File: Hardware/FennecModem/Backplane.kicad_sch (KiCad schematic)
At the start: 4 parts, among them U301 NCP1117-12_SOT223

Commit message: Route!
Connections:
- net SPI_SDO: now reaches U302.17 (SPI_SD0)
- no-connect marks 12 -> 11
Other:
- moved on the sheet: C302, C303, U301, U302

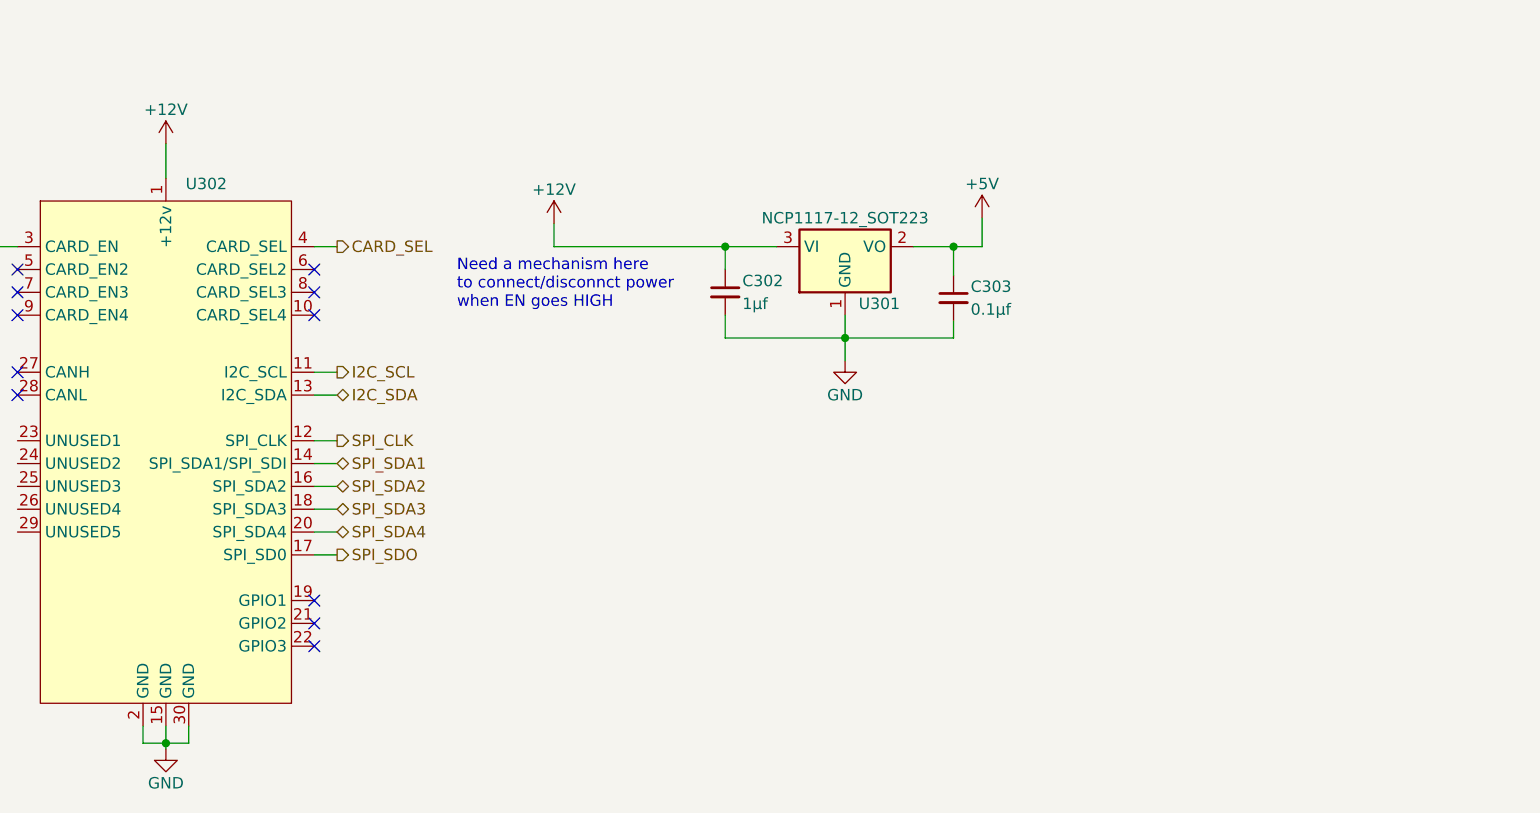
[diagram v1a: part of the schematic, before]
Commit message: Change all power switching
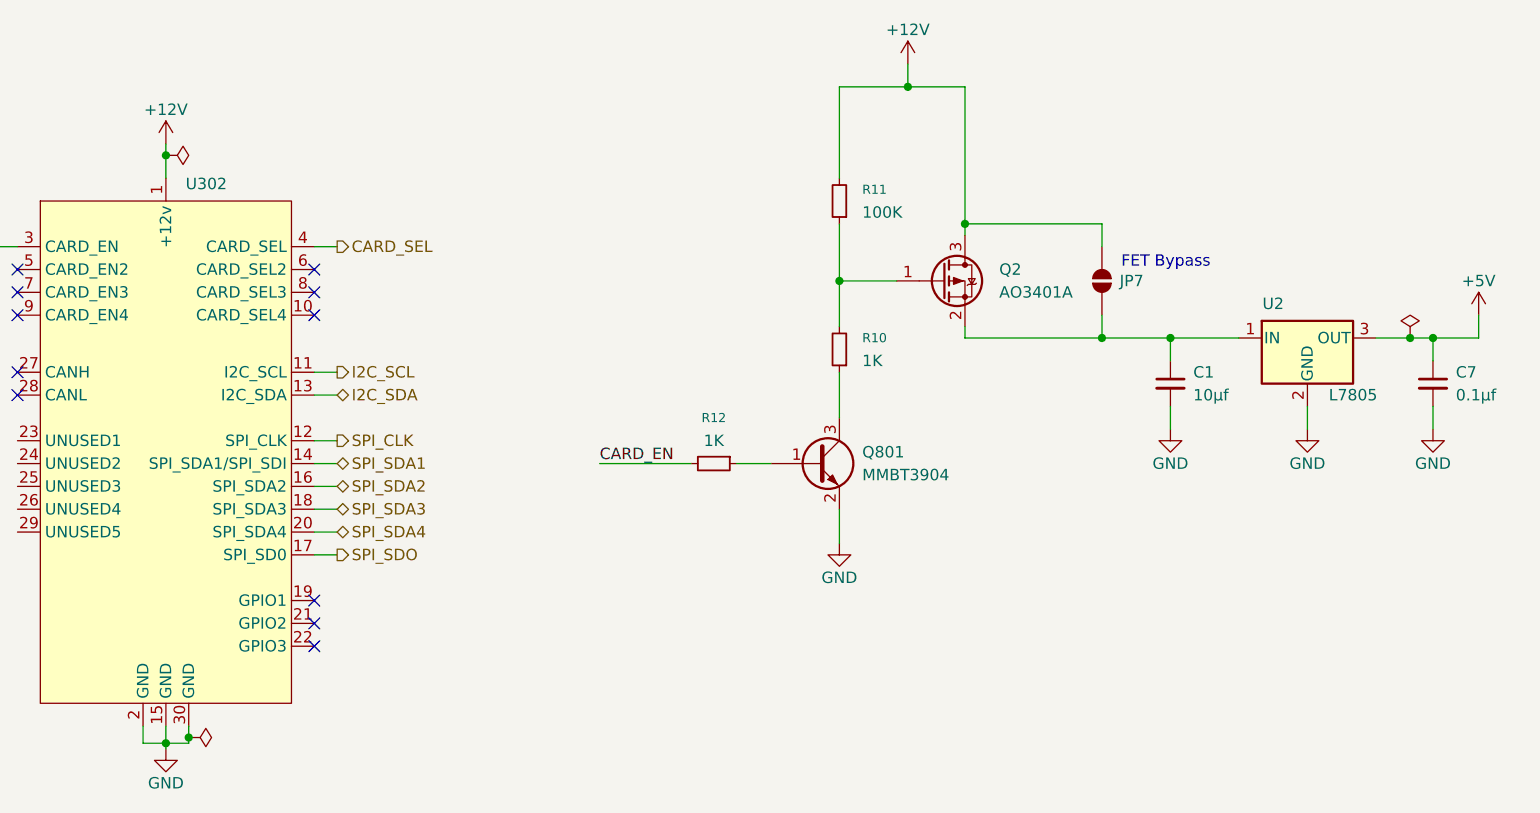
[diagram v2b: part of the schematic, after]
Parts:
- removed C302: 1μf, Capacitor_SMD:C_0805_2012Metric, symbol Device:C_Small
- removed C303: 0.1μf, Capacitor_SMD:C_0805_2012Metric, symbol Device:C_Small
- removed U301: NCP1117-12_SOT223, Package_TO_SOT_SMD:SOT-223-3_TabPin2, symbol Regulator_Linear:NCP1117-12_SOT223
- added C1: 10μf, Capacitor_SMD:C_0805_2012Metric, symbol Device:C_Small
- added C7: 0.1μf, Capacitor_SMD:C_0805_2012Metric, symbol Device:C_Small
- added JP7: SolderJumper_2_Open, Jumper:SolderJumper-2_P1.3mm_Open_TrianglePad1.0x1.5mm, symbol Jumper:SolderJumper_2_Open
- added Q2: AO3401A, Package_TO_SOT_SMD:SOT-23, symbol Transistor_FET:AO3401A
- added Q801: MMBT3904, Package_TO_SOT_SMD:SOT-23, symbol Transistor_BJT:MMBT3904
- added R10, R12: 1K, Resistor_SMD:R_0805_2012Metric, symbol Device:R_Small
- added R11: 100K, Resistor_SMD:R_0805_2012Metric, symbol Device:R_Small
- added U2: L7805, Package_TO_SOT_THT:TO-220-3_Horizontal_TabDown, symbol Regulator_Linear:L7805
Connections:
- net +12V: now also JP7.1 (A), Q2.3 (D), R11.2
- net +5V: now also C7.1, U2.3 (OUT)
- net CARD_EN: now also R12.2
- net GND: now also C1.2, C7.2, Q801.2 (E), U2.2 (GND)
- new net: Q801.3 (C), R10.1
- new net: Q2.1 (G), R10.2, R11.1
- new net: Q801.1 (B), R12.1
- new net: C1.1, JP7.2 (B), Q2.2 (S), U2.1 (IN)
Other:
- note added: "FET Bypass"
- note removed: "Need a mechanism here to connect/disconnct power when EN goes HIGH"

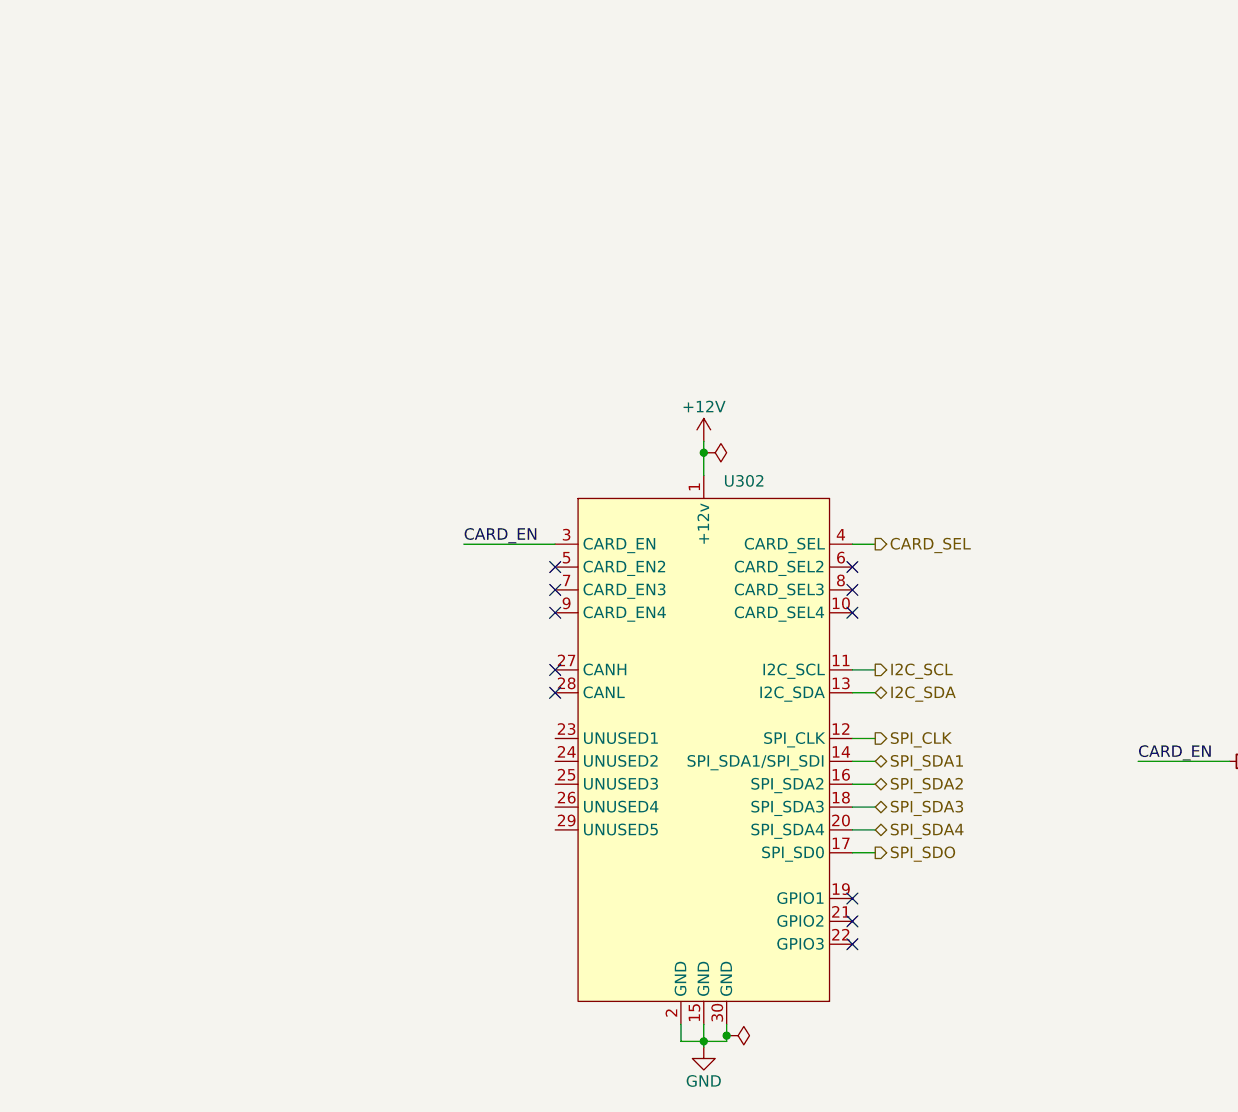
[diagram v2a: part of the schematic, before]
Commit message: add jumpers and bump kicad libs
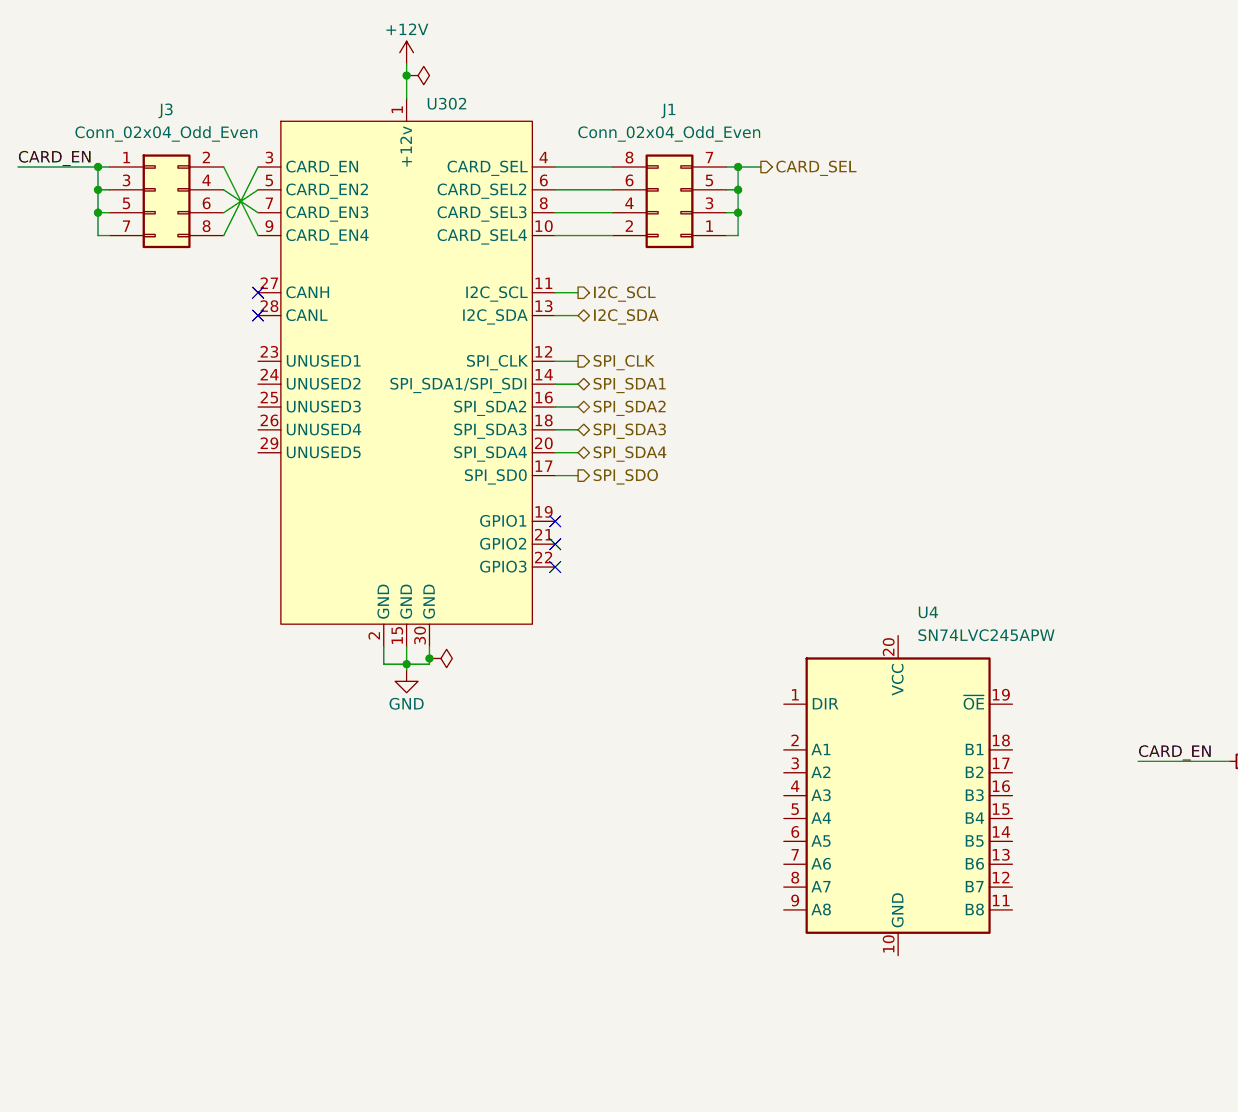
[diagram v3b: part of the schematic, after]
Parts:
- added J1, J3: Conn_02x04_Odd_Even, Connector_PinHeader_2.54mm:PinHeader_2x04_P2.54mm_Vertical, symbol Connector_Generic:Conn_02x04_Odd_Even
- added U4: SN74LVC245APW, Package_SO:TSSOP-20_4.4x6.5mm_P0.65mm, symbol Logic_LevelTranslator:SN74LVC245APW
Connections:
- net CARD_EN: now also J3.1 (Pin_1), J3.3 (Pin_3), J3.5 (Pin_5), J3.7 (Pin_7); no longer U302.3 (CARD_EN)
- net CARD_SEL: now also J1.1 (Pin_1), J1.3 (Pin_3), J1.5 (Pin_5), J1.7 (Pin_7); no longer U302.4 (CARD_SEL)
- net at U302.10 (CARD_SEL4): now also J1.2 (Pin_2)
- net at U302.5 (CARD_EN2): now also J3.6 (Pin_6)
- net at U302.6 (CARD_SEL2): now also J1.6 (Pin_6)
- net at U302.7 (CARD_EN3): now also J3.4 (Pin_4)
- net at U302.8 (CARD_SEL3): now also J1.4 (Pin_4)
- net at U302.9 (CARD_EN4): now also J3.2 (Pin_2)
- new net: J3.8 (Pin_8), U302.3 (CARD_EN)
- new net: J1.8 (Pin_8), U302.4 (CARD_SEL)
- no-connect marks 11 -> 5
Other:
- moved on the sheet: U302

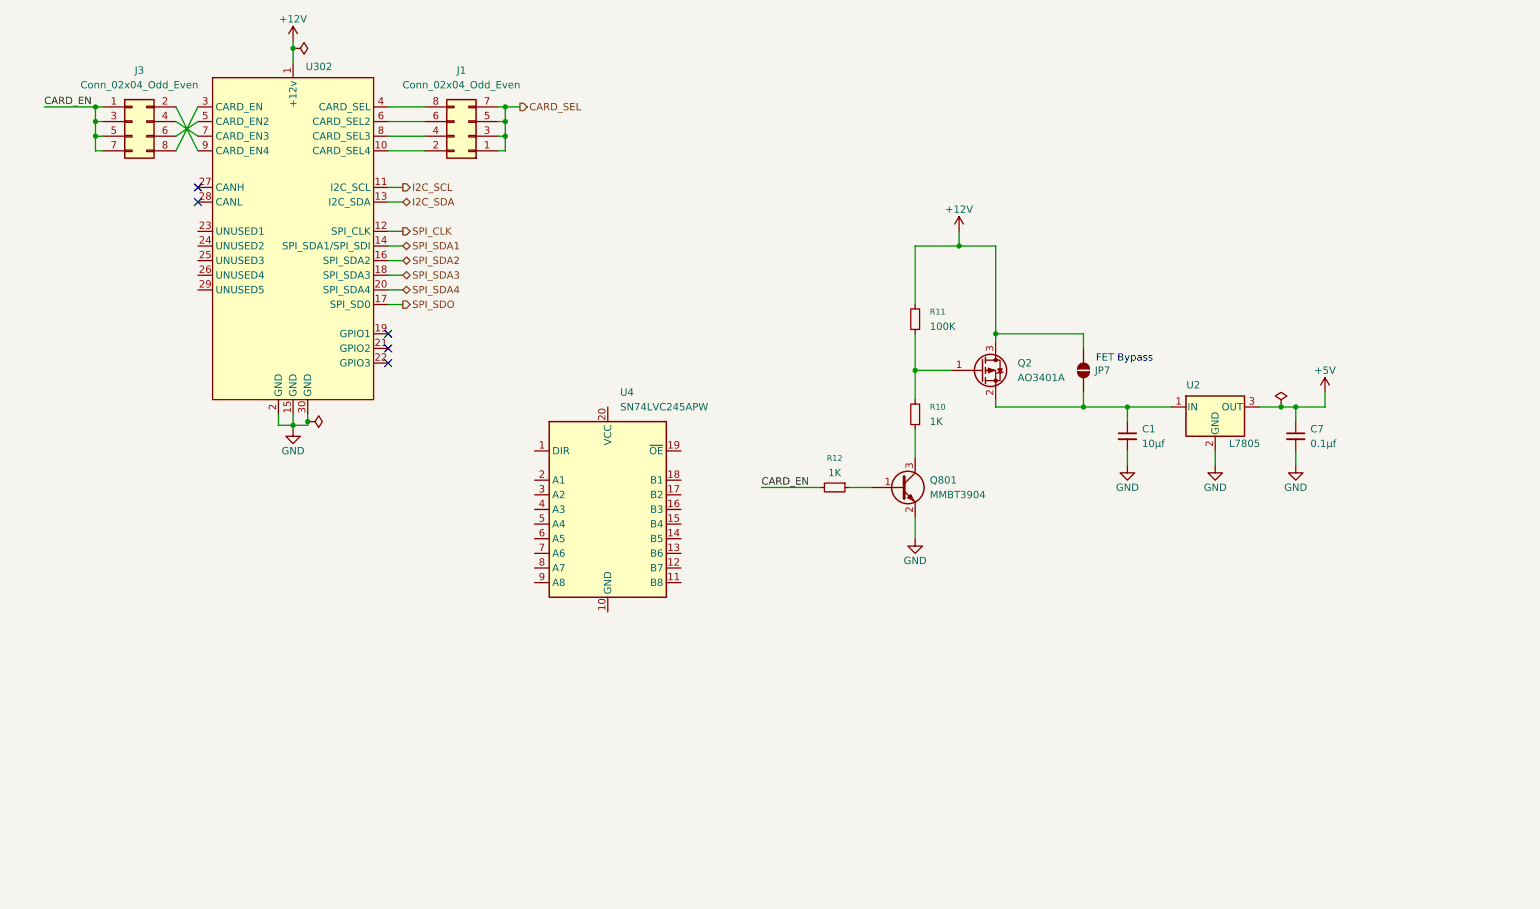
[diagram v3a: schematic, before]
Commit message: Add all nets
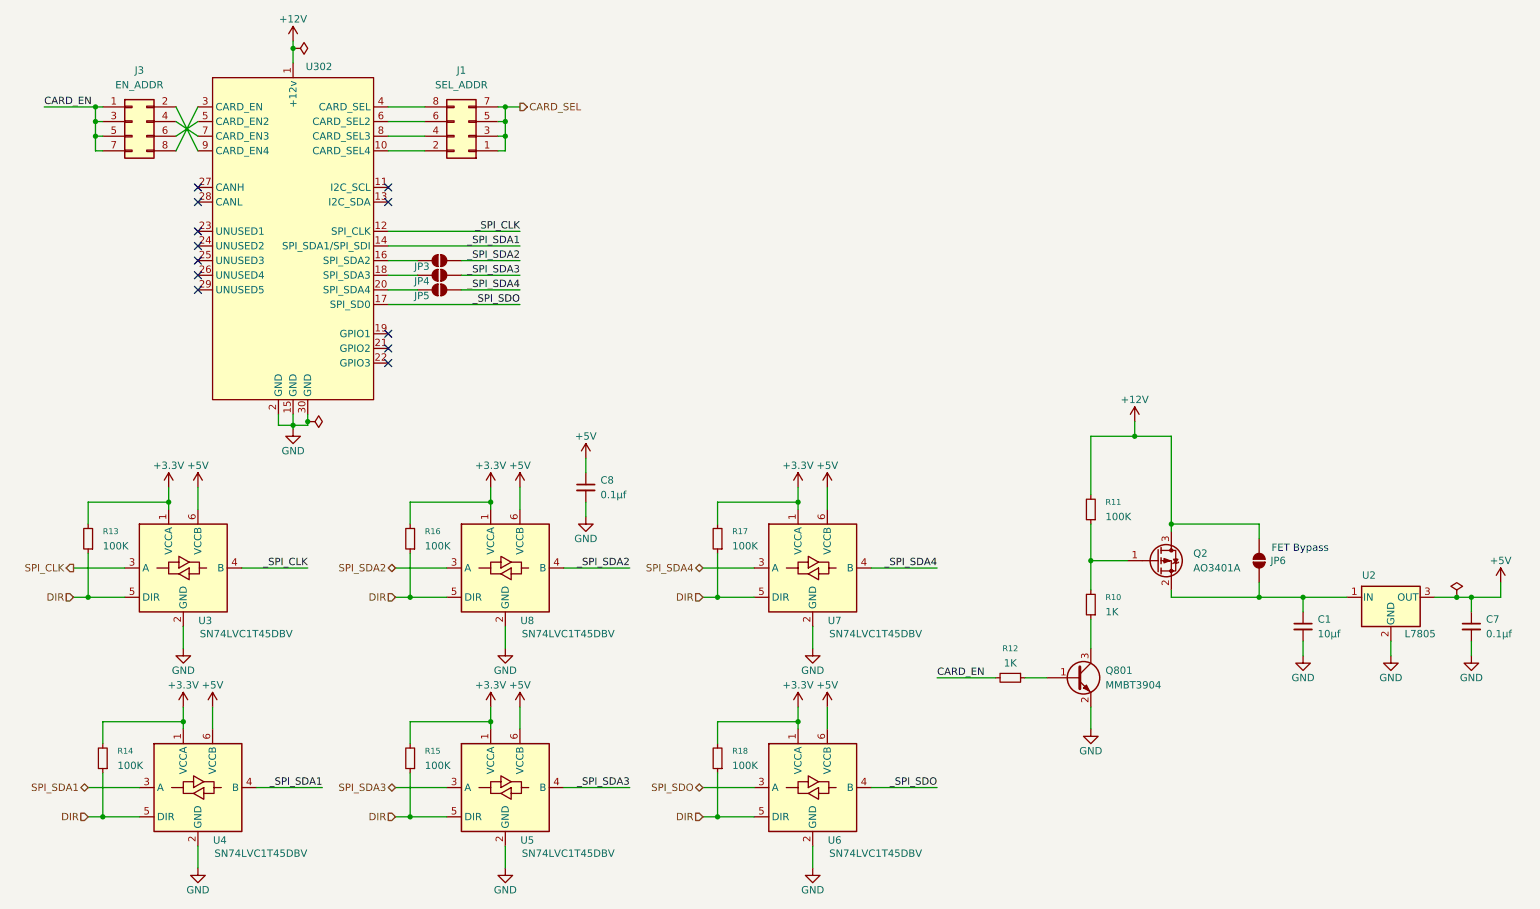
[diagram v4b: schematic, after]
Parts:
- removed U4: SN74LVC245APW, Package_SO:TSSOP-20_4.4x6.5mm_P0.65mm, symbol Logic_LevelTranslator:SN74LVC245APW
- added C8: 0.1μf, Capacitor_SMD:C_0805_2012Metric, symbol Device:C_Small
- added JP3, JP4, JP5: SolderJumper_2_Open, Jumper:SolderJumper-2_P1.3mm_Open_TrianglePad1.0x1.5mm, symbol Jumper:SolderJumper_2_Open
- added R13, R14, R15, R16, R17, R18: 100K, Resistor_SMD:R_0805_2012Metric, symbol Device:R_Small
- added U3, U4, U5, U6, U7, U8: SN74LVC1T45DBV, Package_TO_SOT_SMD:SOT-23-6, symbol Logic_LevelTranslator:SN74LVC1T45DBV
- J1: value Conn_02x04_Odd_Even -> SEL_ADDR
- J3: value Conn_02x04_Odd_Even -> EN_ADDR
- renumbered JP7 to JP6
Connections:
- net +5V: now also C8.1, U3.6 (VCCB), U4.6 (VCCB), U5.6 (VCCB), U6.6 (VCCB), U7.6 (VCCB), U8.6 (VCCB)
- net GND: now also C8.2, U3.2 (GND), U4.2 (GND), U5.2 (GND), U6.2 (GND), U7.2 (GND), U8.2 (GND)
- net SPI_CLK: now also U3.3 (A); no longer U302.12 (SPI_CLK)
- net SPI_SDA1: now also U4.3 (A); no longer U302.14 (SPI_SDA1/SPI_SDI)
- net SPI_SDA2: now also U8.3 (A); no longer U302.16 (SPI_SDA2)
- net SPI_SDA3: now also U5.3 (A); no longer U302.18 (SPI_SDA3)
- net SPI_SDA4: now also U7.3 (A); no longer U302.20 (SPI_SDA4)
- net SPI_SDO: now also U6.3 (A); no longer U302.17 (SPI_SD0)
- net I2C_SCL: no longer names the net of U302.11 (I2C_SCL)
- net I2C_SDA: no longer names the net of U302.13 (I2C_SDA)
- new net: JP3.2 (B), U302.16 (SPI_SDA2)
- new net: JP4.2 (B), U302.18 (SPI_SDA3)
- new net: JP5.2 (B), U302.20 (SPI_SDA4)
- new net +3.3V: R13.2, R14.2, R15.2, R16.2, R17.2, R18.2, U3.1 (VCCA), U4.1 (VCCA), U5.1 (VCCA), U6.1 (VCCA), U7.1 (VCCA), U8.1 (VCCA)
- new net DIR: R13.1, R14.1, R15.1, R16.1, R17.1, R18.1, U3.5 (DIR), U4.5 (DIR), U5.5 (DIR), U6.5 (DIR), U7.5 (DIR), U8.5 (DIR)
- new net _SPI_CLK: U3.4 (B), U302.12 (SPI_CLK)
- new net _SPI_SDA1: U302.14 (SPI_SDA1/SPI_SDI), U4.4 (B)
- new net _SPI_SDA2: JP3.1 (A), U8.4 (B)
- new net _SPI_SDA3: JP4.1 (A), U5.4 (B)
- new net _SPI_SDA4: JP5.1 (A), U7.4 (B)
- new net _SPI_SDO: U302.17 (SPI_SD0), U6.4 (B)
- no-connect marks 5 -> 12
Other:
- moved on the sheet: C1, C7, JP6, Q2, Q801, R10, R11, R12, U2
